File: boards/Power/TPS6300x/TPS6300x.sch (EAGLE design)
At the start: 12 parts

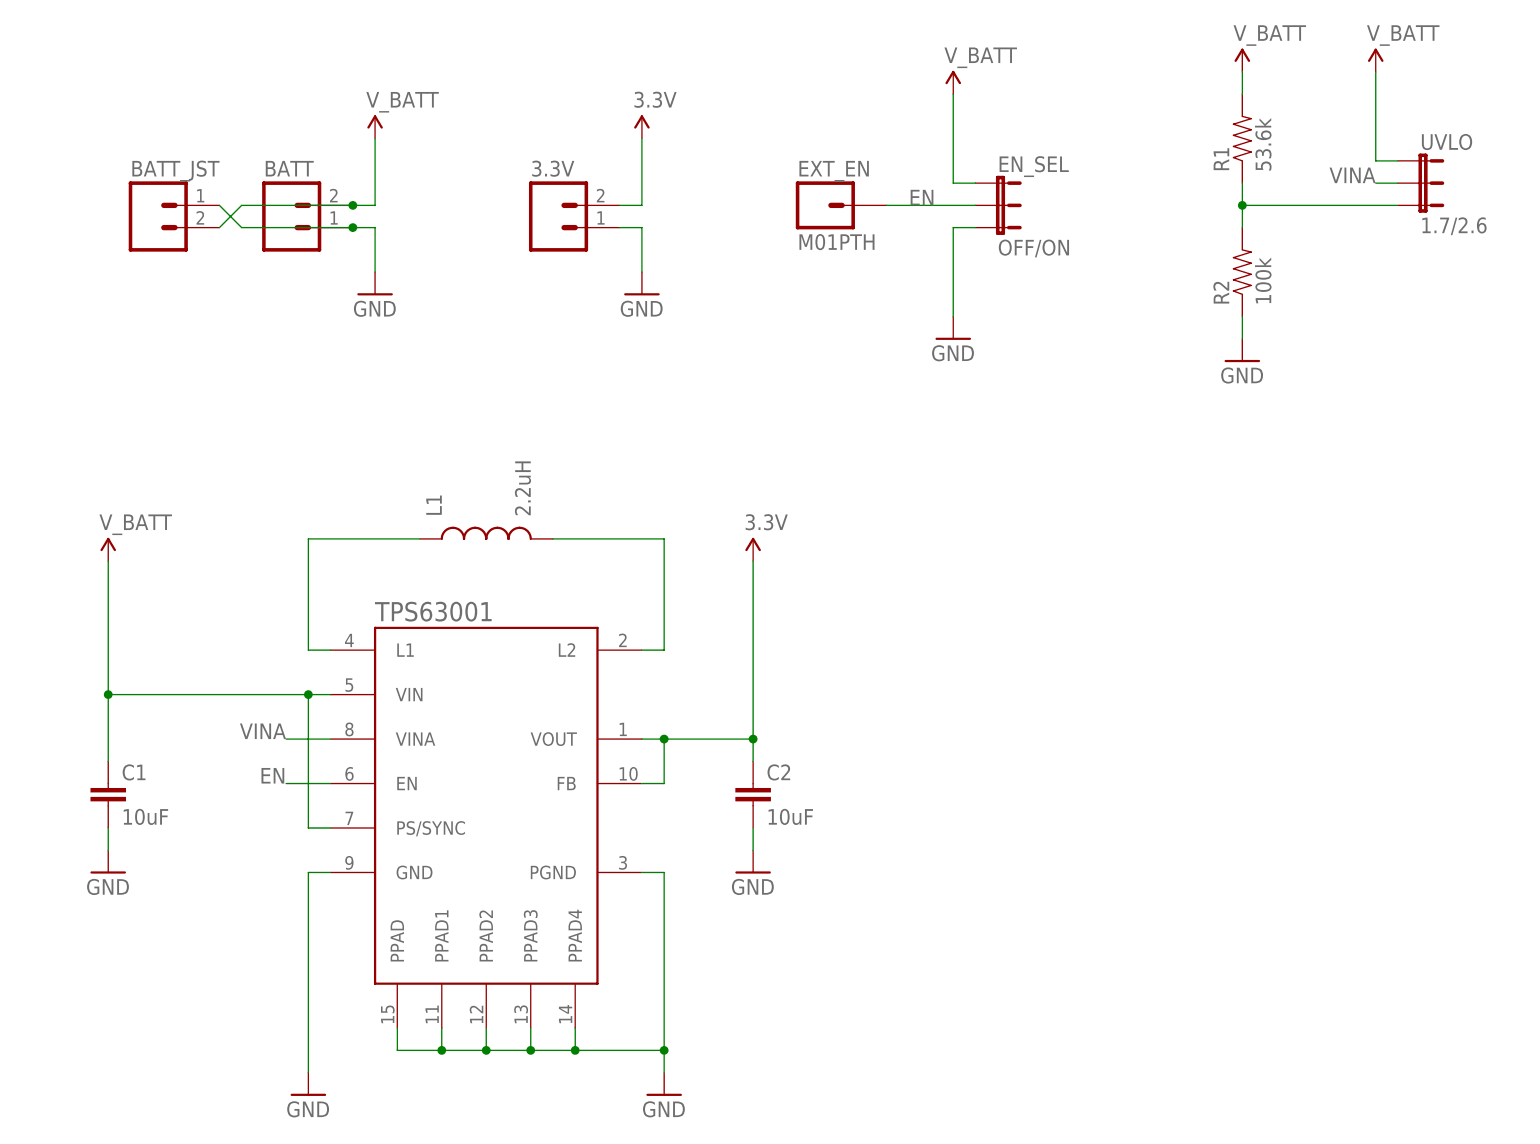
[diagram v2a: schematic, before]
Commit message: Removed voltage divider on power board
Vina wasn't the place to do a voltage divider, and I realized that I
really didn't need one -- I don't want a cutoff for the Lithium primary
batteries, and the Li-Ion batteries have a built-in low-voltage cutoff.
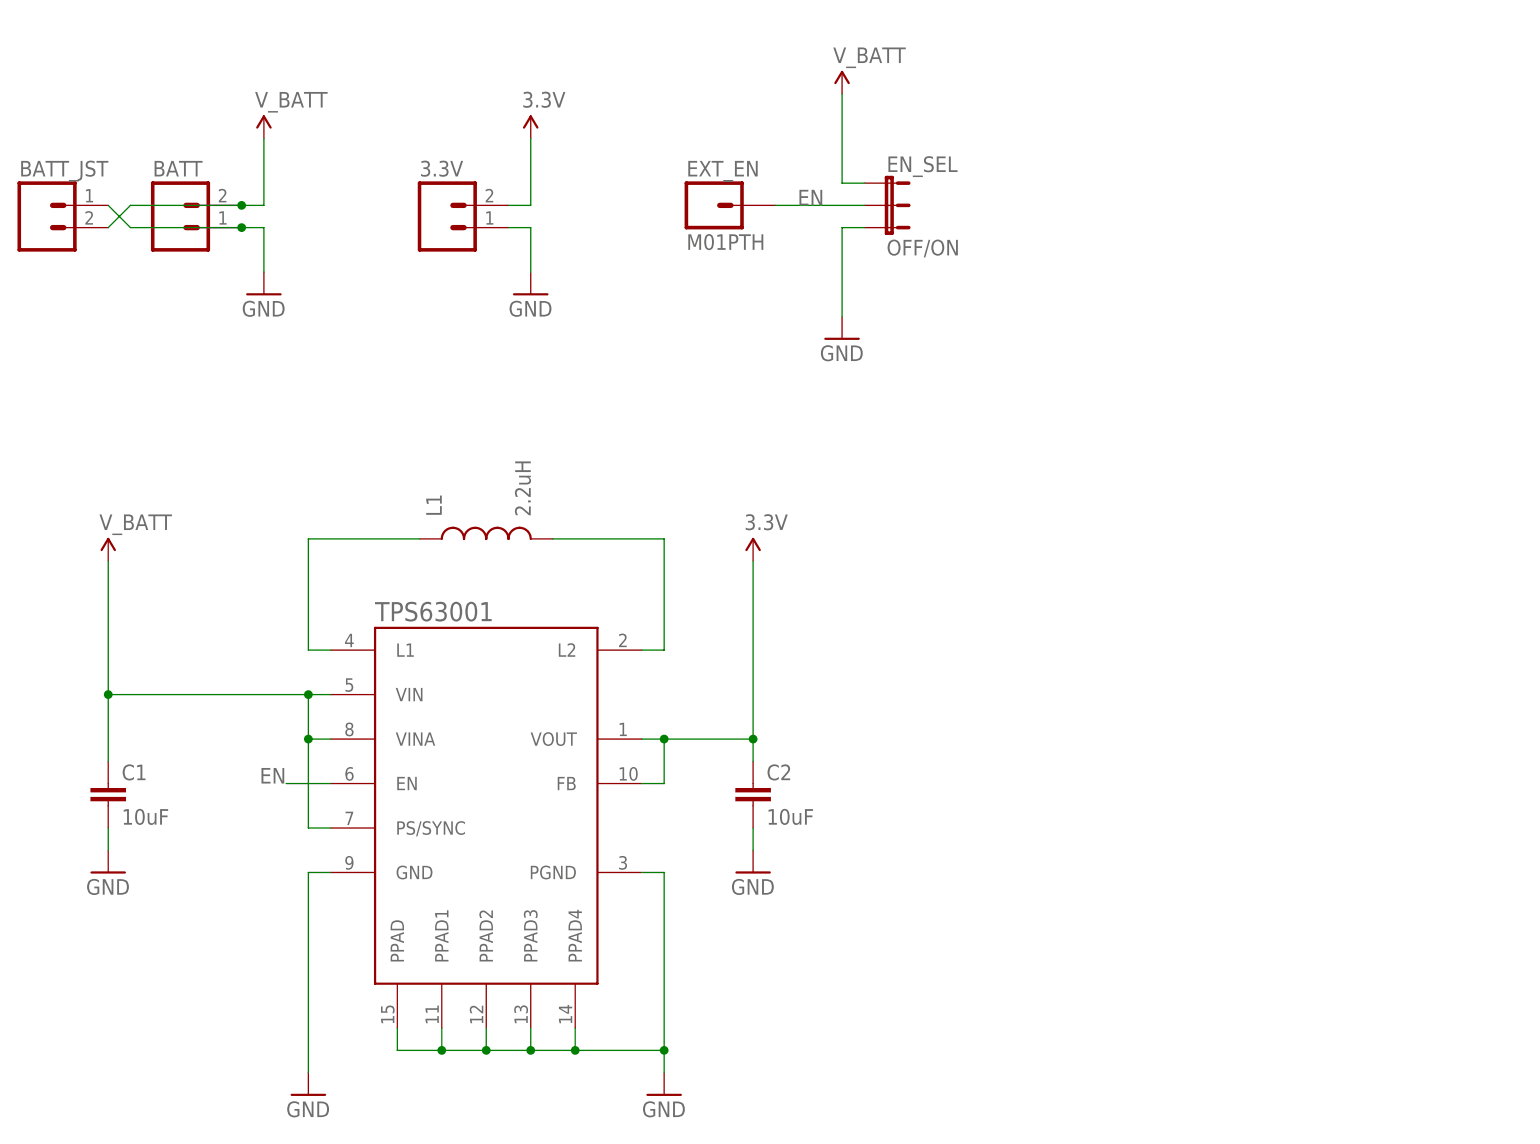
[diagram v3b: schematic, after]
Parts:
- removed R1: 53.6k, SparkFun-Passives:RESISTOR0805-RES
- removed R2: 100k, SparkFun-Passives:RESISTOR0805-RES
- removed UVLO: 1.7/2.6, SparkFun-Passives:JUMPER-3SMD
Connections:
- removed net N$4: R1.1, R2.2, UVLO.3
- removed net VINA: TPS63001.VINA, UVLO.2
- net 1.8V: now also TPS63001.VINA; no longer R1.2, UVLO.1
- net GND: no longer R2.1
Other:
- moved on the sheet: 3.3V, BATT, BATT_JST, EN_SEL, EXT_EN
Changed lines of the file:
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@@
 <part name="GND9" library="SparkFun-Aesthetics" deviceset="GND" device=""/>
 <part name="L1" library="OpenSpace" deviceset="INDUCTOR" device="-VLF4012A" value="2.2uH"/>
-<part name="GND19" library="SparkFun-Aesthetics" deviceset="GND" device=""/>
-<part name="U$6" library="SparkFun-Aesthetics" deviceset="V_BATT" device=""/>
-<part name="R1" library="SparkFun-Passives" deviceset="RESISTOR" device="0805-RES" value="53.6k"/>
-<part name="R2" library="SparkFun-Passives" deviceset="RESISTOR" device="0805-RES" value="100k"/>
 <part name="EXT_EN" library="SparkFun-Connectors" deviceset="M01" device="PTH"/>
 <part name="EN_SEL" library="SparkFun-Passives" deviceset="JUMPER-3" device="SMD" value="OFF/ON"/>
 <part name="U$1" library="SparkFun-Aesthetics" deviceset="V_BATT" device=""/>
 <part name="GND3" library="SparkFun-Aesthetics" deviceset="GND" device=""/>
-<part name="UVLO" library="SparkFun-Passives" deviceset="JUMPER-3" device="SMD" value="1.7/2.6"/>
-<part name="U$3" library="SparkFun-Aesthetics" deviceset="V_BATT" device=""/>
 </parts>
 <sheets>
@@
 <instance part="P+1" gate="G$1" x="73.66" y="81.28"/>
 <instance part="U$2" gate="G$1" x="0" y="81.28"/>
-<instance part="BATT" gate="G$1" x="20.32" y="119.38"/>
-<instance part="3.3V" gate="G$1" x="50.8" y="119.38"/>
-<instance part="BATT_JST" gate="G$1" x="5.08" y="119.38"/>
-<instance part="U$4" gate="G$1" x="30.48" y="129.54"/>
-<instance part="P+2" gate="G$1" x="60.96" y="129.54"/>
-<instance part="GND5" gate="1" x="30.48" y="111.76"/>
-<instance part="GND6" gate="1" x="60.96" y="111.76"/>
+<instance part="BATT" gate="G$1" x="7.62" y="119.38"/>
+<instance part="3.3V" gate="G$1" x="38.1" y="119.38"/>
+<instance part="BATT_JST" gate="G$1" x="-7.62" y="119.38"/>
+<instance part="U$4" gate="G$1" x="17.78" y="129.54"/>
+<instance part="P+2" gate="G$1" x="48.26" y="129.54"/>
+<instance part="GND5" gate="1" x="17.78" y="111.76"/>
+<instance part="GND6" gate="1" x="48.26" y="111.76"/>
 <instance part="C1" gate="G$1" x="0" y="50.8"/>
 <instance part="C2" gate="G$1" x="73.66" y="50.8"/>
@@
 <instance part="GND9" gate="1" x="73.66" y="45.72"/>
 <instance part="L1" gate="G$1" x="43.18" y="83.82" rot="R90"/>
-<instance part="GND19" gate="1" x="129.54" y="104.14"/>
-<instance part="U$6" gate="G$1" x="129.54" y="137.16"/>
-<instance part="R1" gate="G$1" x="129.54" y="129.54" rot="R90"/>
-<instance part="R2" gate="G$1" x="129.54" y="114.3" rot="R90"/>
-<instance part="EXT_EN" gate="G$1" x="81.28" y="121.92"/>
-<instance part="EN_SEL" gate="G$1" x="101.6" y="124.46" rot="R270"/>
-<instance part="U$1" gate="G$1" x="96.52" y="134.62"/>
-<instance part="GND3" gate="1" x="96.52" y="106.68"/>
-<instance part="UVLO" gate="G$1" x="149.86" y="127" rot="R270"/>
-<instance part="U$3" gate="G$1" x="144.78" y="137.16"/>
+<instance part="EXT_EN" gate="G$1" x="68.58" y="121.92"/>
+<instance part="EN_SEL" gate="G$1" x="88.9" y="124.46" rot="R270"/>
+<instance part="U$1" gate="G$1" x="83.82" y="134.62"/>
+<instance part="GND3" gate="1" x="83.82" y="106.68"/>
 </instances>
 <busses>
@@
 <pinref part="BATT" gate="G$1" pin="1"/>
 <pinref part="GND5" gate="1" pin="GND"/>
-<wire x1="27.94" y1="119.38" x2="30.48" y2="119.38" width="0.1524" layer="91"/>
-<wire x1="30.48" y1="119.38" x2="30.48" y2="114.3" width="0.1524" layer="91"/>
-<wire x1="27.94" y1="119.38" x2="15.24" y2="119.38" width="0.1524" layer="91"/>
-<junction x="27.94" y="119.38"/>
+<wire x1="15.24" y1="119.38" x2="17.78" y2="119.38" width="0.1524" layer="91"/>
+<wire x1="17.78" y1="119.38" x2="17.78" y2="114.3" width="0.1524" layer="91"/>
+<wire x1="15.24" y1="119.38" x2="2.54" y2="119.38" width="0.1524" layer="91"/>
+<junction x="15.24" y="119.38"/>
 <pinref part="BATT_JST" gate="G$1" pin="2"/>
-<wire x1="15.24" y1="119.38" x2="12.7" y2="121.92" width="0.1524" layer="91"/>
+<wire x1="2.54" y1="119.38" x2="0" y2="121.92" width="0.1524" layer="91"/>
 </segment>
 <segment>
 <pinref part="3.3V" gate="G$1" pin="1"/>
 <pinref part="GND6" gate="1" pin="GND"/>
-<wire x1="58.42" y1="119.38" x2="60.96" y2="119.38" width="0.1524" layer="91"/>
-<wire x1="60.96" y1="119.38" x2="60.96" y2="114.3" width="0.1524" layer="91"/>
+<wire x1="45.72" y1="119.38" x2="48.26" y2="119.38" width="0.1524" layer="91"/>
+<wire x1="48.26" y1="119.38" x2="48.26" y2="114.3" width="0.1524" layer="91"/>
 </segment>
 <segment>
@@
 </segment>
 <segment>
-<pinref part="R2" gate="G$1" pin="1"/>
-<pinref part="GND19" gate="1" pin="GND"/>
-<wire x1="129.54" y1="106.68" x2="129.54" y2="109.22" width="0.1524" layer="91"/>
-</segment>
-<segment>
 <pinref part="EN_SEL" gate="G$1" pin="3"/>
-<wire x1="99.06" y1="119.38" x2="96.52" y2="119.38" width="0.1524" layer="91"/>
-<wire x1="96.52" y1="119.38" x2="96.52" y2="109.22" width="0.1524" layer="91"/>
+<wire x1="86.36" y1="119.38" x2="83.82" y2="119.38" width="0.1524" layer="91"/>
+<wire x1="83.82" y1="119.38" x2="83.82" y2="109.22" width="0.1524" layer="91"/>
 <pinref part="GND3" gate="1" pin="GND"/>
 </segment>
@@
 <pinref part="3.3V" gate="G$1" pin="2"/>
 <pinref part="P+2" gate="G$1" pin="3.3V"/>
-<wire x1="58.42" y1="121.92" x2="60.96" y2="121.92" width="0.1524" layer="91"/>
-<wire x1="60.96" y1="121.92" x2="60.96" y2="129.54" width="0.1524" layer="91"/>
+<wire x1="45.72" y1="121.92" x2="48.26" y2="121.92" width="0.1524" layer="91"/>
+<wire x1="48.26" y1="121.92" x2="48.26" y2="129.54" width="0.1524" layer="91"/>
 </segment>
 </net>
@@
 <pinref part="TPS63001" gate="TPS6300X" pin="PS/SYNC"/>
 <wire x1="25.4" y1="50.8" x2="22.86" y2="50.8" width="0.1524" layer="91"/>
-<wire x1="22.86" y1="50.8" x2="22.86" y2="66.04" width="0.1524" layer="91"/>
+<wire x1="22.86" y1="50.8" x2="22.86" y2="60.96" width="0.1524" layer="91"/>
 <pinref part="C1" gate="G$1" pin="+"/>
+<wire x1="22.86" y1="60.96" x2="22.86" y2="66.04" width="0.1524" layer="91"/>
 <wire x1="0" y1="58.42" x2="0" y2="66.04" width="0.1524" layer="91"/>
 <junction x="0" y="66.04"/>
+<pinref part="TPS63001" gate="TPS6300X" pin="VINA"/>
+<wire x1="25.4" y1="60.96" x2="22.86" y2="60.96" width="0.1524" layer="91"/>
+<junction x="22.86" y="60.96"/>
 </segment>
 <segment>
 <pinref part="BATT" gate="G$1" pin="2"/>
 <pinref part="U$4" gate="G$1" pin="1.8V"/>
-<wire x1="27.94" y1="121.92" x2="30.48" y2="121.92" width="0.1524" layer="91"/>
-<wire x1="30.48" y1="121.92" x2="30.48" y2="129.54" width="0.1524" layer="91"/>
-<wire x1="27.94" y1="121.92" x2="15.24" y2="121.92" width="0.1524" layer="91"/>
-<junction x="27.94" y="121.92"/>
+<wire x1="15.24" y1="121.92" x2="17.78" y2="121.92" width="0.1524" layer="91"/>
+<wire x1="17.78" y1="121.92" x2="17.78" y2="129.54" width="0.1524" layer="91"/>
+<wire x1="15.24" y1="121.92" x2="2.54" y2="121.92" width="0.1524" layer="91"/>
+<junction x="15.24" y="121.92"/>
 <pinref part="BATT_JST" gate="G$1" pin="1"/>
-<wire x1="15.24" y1="121.92" x2="12.7" y2="119.38" width="0.1524" layer="91"/>
-</segment>
-<segment>
-<pinref part="R1" gate="G$1" pin="2"/>
-<pinref part="U$6" gate="G$1" pin="1.8V"/>
-<wire x1="129.54" y1="137.16" x2="129.54" y2="134.62" width="0.1524" layer="91"/>
+<wire x1="2.54" y1="121.92" x2="0" y2="119.38" width="0.1524" layer="91"/>
 </segment>
 <segment>
 <pinref part="EN_SEL" gate="G$1" pin="1"/>
-<wire x1="99.06" y1="124.46" x2="96.52" y2="124.46" width="0.1524" layer="91"/>
-<wire x1="96.52" y1="124.46" x2="96.52" y2="134.62" width="0.1524" layer="91"/>
+<wire x1="86.36" y1="124.46" x2="83.82" y2="124.46" width="0.1524" layer="91"/>
+<wire x1="83.82" y1="124.46" x2="83.82" y2="134.62" width="0.1524" layer="91"/>
 <pinref part="U$1" gate="G$1" pin="1.8V"/>
-</segment>
-<segment>
-<pinref part="UVLO" gate="G$1" pin="1"/>
-<wire x1="147.32" y1="127" x2="144.78" y2="127" width="0.1524" layer="91"/>
-<wire x1="144.78" y1="127" x2="144.78" y2="137.16" width="0.1524" layer="91"/>
-<pinref part="U$3" gate="G$1" pin="1.8V"/>
 </segment>
 </net>
@@
 <pinref part="EN_SEL" gate="G$1" pin="2"/>
 <pinref part="EXT_EN" gate="G$1" pin="1"/>
-<wire x1="99.06" y1="121.92" x2="88.9" y2="121.92" width="0.1524" layer="91"/>
-<label x="91.44" y="121.92" size="1.778" layer="95"/>
+<wire x1="86.36" y1="121.92" x2="76.2" y2="121.92" width="0.1524" layer="91"/>
+<label x="78.74" y="121.92" size="1.778" layer="95"/>
 </segment>
 </net>
-<net name="VINA" class="0">
-<segment>
-<pinref part="TPS63001" gate="TPS6300X" pin="VINA"/>
-<wire x1="25.4" y1="60.96" x2="20.32" y2="60.96" width="0.1524" layer="91"/>
-<label x="20.32" y="60.96" size="1.778" layer="95" rot="MR0"/>
-</segment>
-<segment>
-<pinref part="UVLO" gate="G$1" pin="2"/>
-<wire x1="147.32" y1="124.46" x2="144.78" y2="124.46" width="0.1524" layer="91"/>
-<label x="144.78" y="124.46" size="1.778" layer="95" rot="MR0"/>
-</segment>
-</net>
-<net name="N$4" class="0">
-<segment>
-<pinref part="UVLO" gate="G$1" pin="3"/>
-<pinref part="R2" gate="G$1" pin="2"/>
-<pinref part="R1" gate="G$1" pin="1"/>
-<wire x1="129.54" y1="124.46" x2="129.54" y2="121.92" width="0.1524" layer="91"/>
-<wire x1="129.54" y1="121.92" x2="129.54" y2="119.38" width="0.1524" layer="91"/>
-<wire x1="147.32" y1="121.92" x2="129.54" y2="121.92" width="0.1524" layer="91"/>
-<junction x="129.54" y="121.92"/>
-</segment>
-</net>
